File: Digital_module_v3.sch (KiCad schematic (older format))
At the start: 74 parts, among them J1 Pow_mng_iface, J2 Fan_mod_iface, J3 Iface_mod_iface, J4 B2B-EH-A, J5 ADC_iface, J6 USB_B_Micro, J7 Pow_mng_pow, J8 DS18B20_iface, Q1 BSS138, Q10 BSS138, Q11 BSS138, Q12 BSS138, Q2 BSS138, Q3 BSS138, Q4 BSS138, Q5 BSS138, Q6 BSS138, Q7 BSS138, Q8 BSS138, Q9 BSS138, U1 PCA9544APW, U2 PCF8563TS, U3 LM1117-3.3, U4 USBLC6-2SC6, Y1 SC-32S 32.768KHz

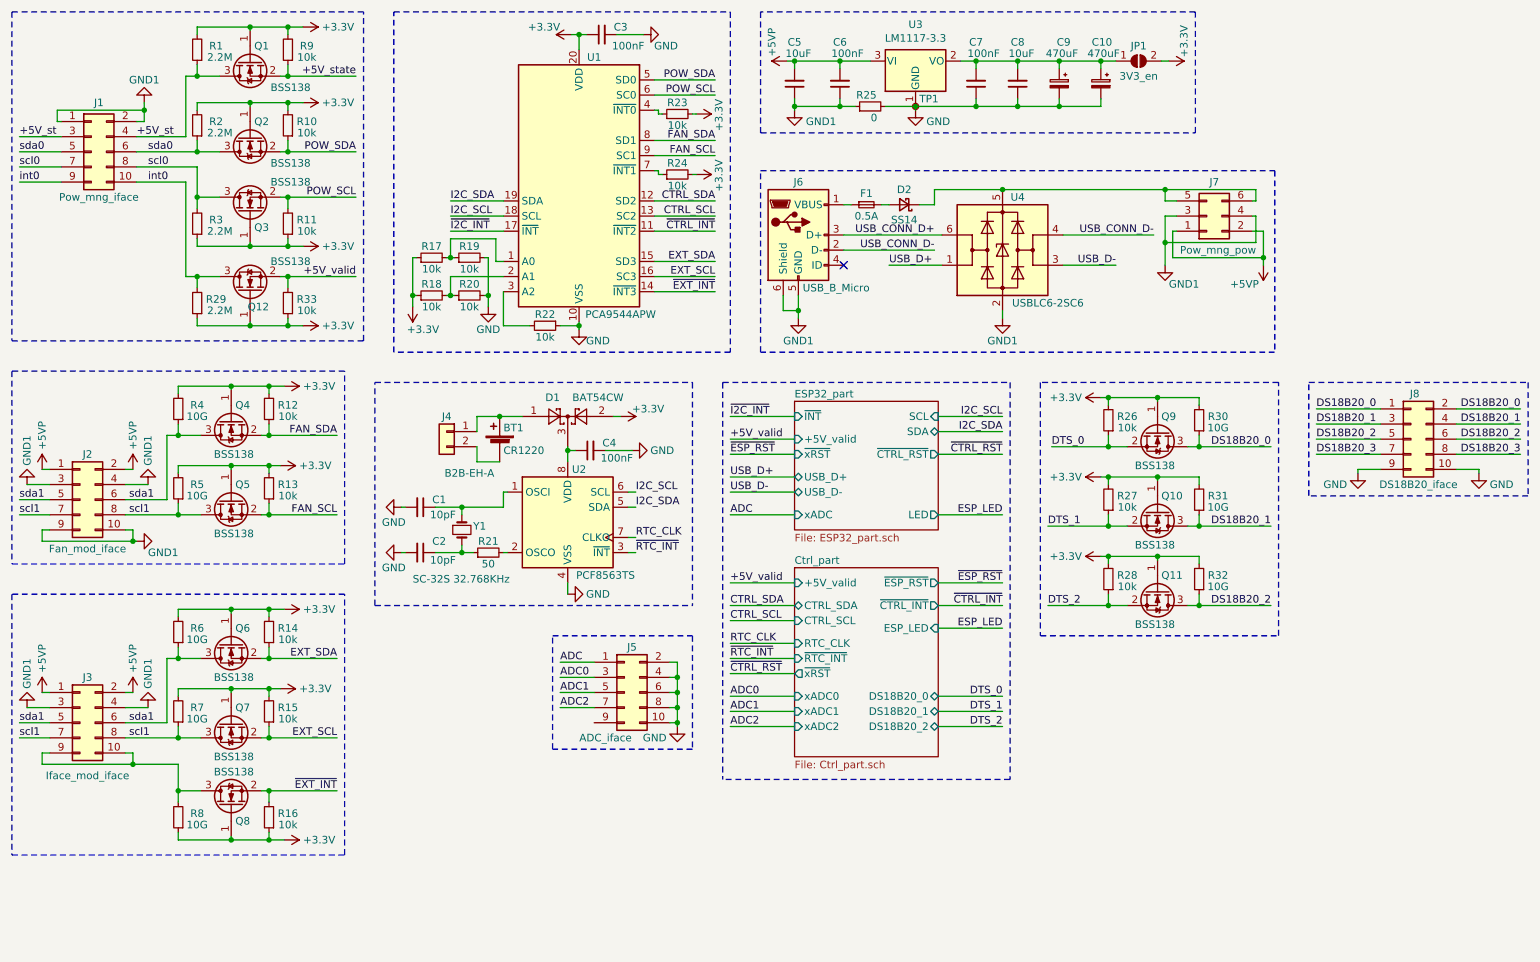
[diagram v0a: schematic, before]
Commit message: Завершена трассировка печатной платы. Исправлены ошибки в схема.
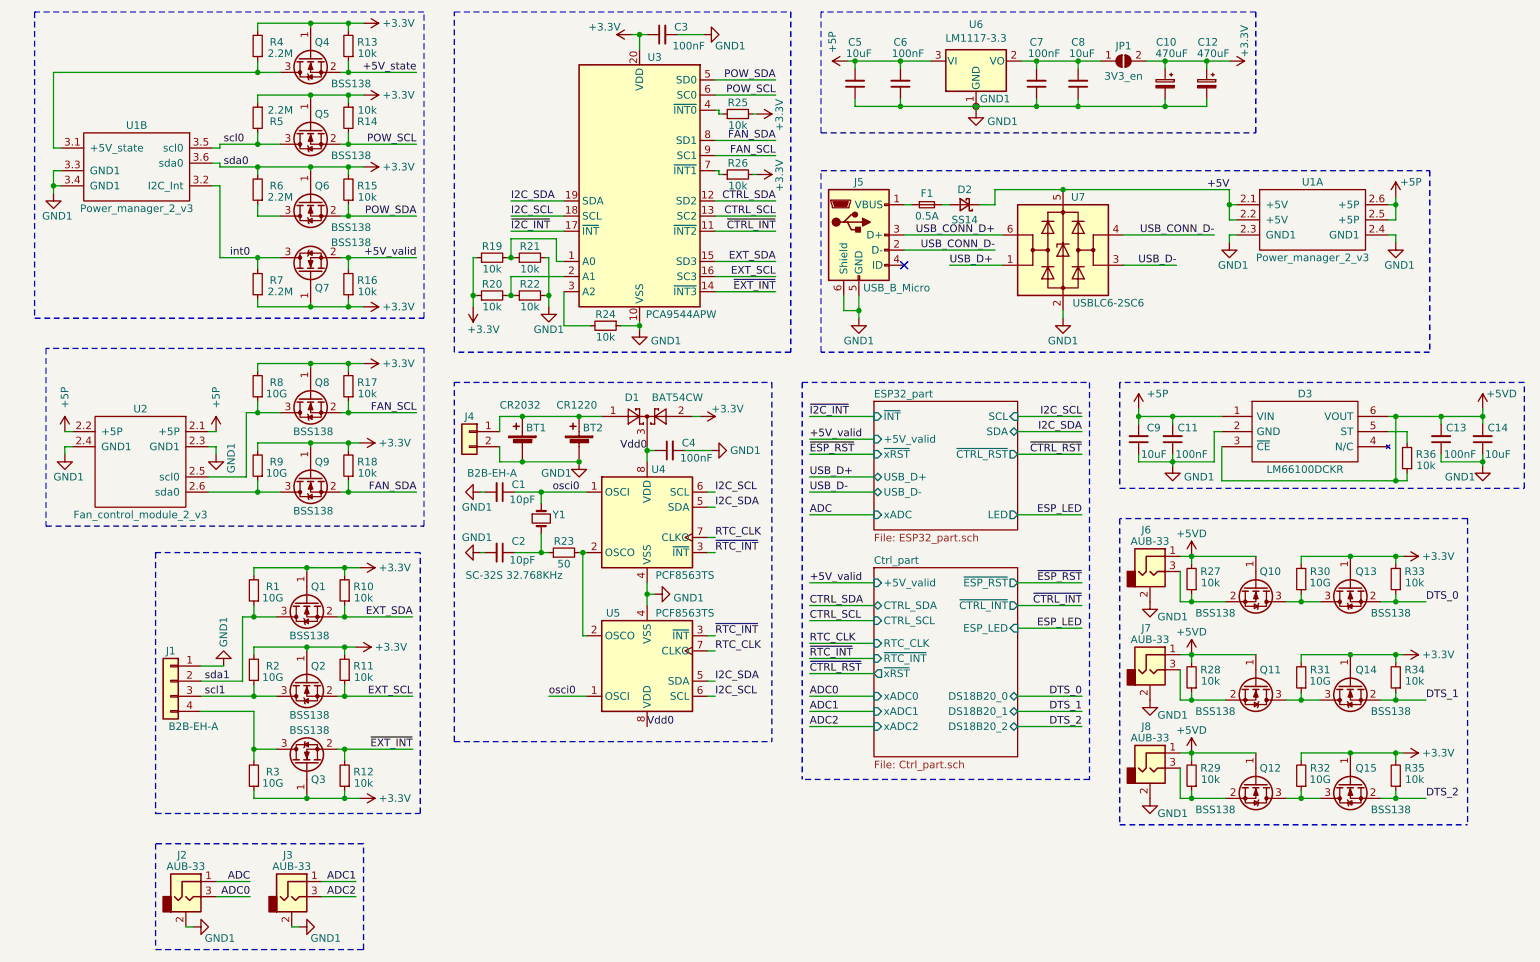
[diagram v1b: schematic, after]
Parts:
- removed J1: Pow_mng_iface, Connector_PinHeader_1.27mm:PinHeader_2x05_P1.27mm_Vertical_SMD, symbol Connector_Generic:Conn_02x05_Odd_Even
- removed J2: Fan_mod_iface, Connector_PinSocket_1.27mm:PinSocket_2x05_P1.27mm_Horizontal, symbol Connector_Generic:Conn_02x05_Odd_Even
- removed J3: Iface_mod_iface, Connector_PinSocket_1.27mm:PinSocket_2x05_P1.27mm_Horizontal, symbol Connector_Generic:Conn_02x05_Odd_Even
- removed J5: ADC_iface, Connector_PinSocket_1.27mm:PinSocket_2x05_P1.27mm_Horizontal, symbol Connector_Generic:Conn_02x05_Odd_Even
- removed J7: Pow_mng_pow, Connector_PinHeader_1.27mm:PinHeader_2x03_P1.27mm_Vertical_SMD, symbol Connector_Generic:Conn_02x03_Odd_Even
- removed J8: DS18B20_iface, Connector_PinSocket_1.27mm:PinSocket_2x05_P1.27mm_Horizontal, symbol Connector_Generic:Conn_02x05_Odd_Even
- removed Q9: BSS138, Package_TO_SOT_SMD:SOT-23, symbol Transistor_FET:BSS138
- removed R25: 0, Resistor_SMD:R_0603_1608Metric, symbol Device:R_Small
- removed R26: 10k, Resistor_SMD:R_0603_1608Metric, symbol Device:R_Small
- added BT1: CR2032, Modules:CR2032BS51, symbol Device:Battery_Cell
- added C11, C13: 100nF, Capacitor_SMD:C_0603_1608Metric, symbol Device:C_Small
- added C14, C9: 10uF, Capacitor_SMD:C_0603_1608Metric, symbol Device:C_Small
- added D3: LM66100DCKR, SOP65P210X110-6N, symbol Modules:LM66100DCKR
- added J1: B2B-EH-A, Connector_JST:JST_EH_S4B-EH_1x04_P2.50mm_Horizontal, symbol Connector_Generic:Conn_01x04
- added J2, J3, J6, J7, J8: AUB-33, Modules:AUB-33, symbol Modules:AUB-33
- added Q12, Q13, Q14, Q15: BSS138, Package_TO_SOT_SMD:SOT-23, symbol Transistor_FET:BSS138
- added R29, R33, R34, R35, R36: 10k, Resistor_SMD:R_0603_1608Metric, symbol Device:R_Small
- added U1: Power_manager_2_v3, Modules:Power_manager_2_v3, symbol Modules:Power_manager_2_v3
- added U2: Fan_control_module_2_v3, Modules:Fan_controller_2_v3, symbol Modules:Fan_control_module_2_v3
- added U5: PCF8563TS, Package_SO:SO-8_3.9x4.9mm_P1.27mm, symbol Timer_RTC:PCF8563TS
- GND1: renamed from TP1; value GND -> GND1
- renumbered BT1 to BT2, C9 to C10, C10 to C12, J6 to J5, Q6 to Q1, Q7 to Q2, Q8 to Q3, Q1 to Q4, Q3 to Q5, Q2 to Q6, Q12 to Q7, Q4 to Q8, Q5 to Q9, R6 to R1, R14 to R10, R15 to R11, R16 to R12, R9 to R13, R11 to R14, R10 to R15, R33 to R16, R12 to R17, R13 to R18, R17 to R19, R7 to R2, R18 to R20, R19 to R21, R20 to R22, R21 to R23, R22 to R24, R23 to R25, R24 to R26, R8 to R3, R1 to R4, R3 to R5, R2 to R6, R29 to R7, R4 to R8, R5 to R9, U1 to U3, U2 to U4, U3 to U6, U4 to U7
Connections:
- net GND is gone; now on net GND1: C1.2, C10.2, C12.2, C2.2, C3.2, C4.2, C7.1, C8.1, GND1.1, R21.2, R22.2, R24.1, U3.10 (VSS), U4.4 (VSS), U6.1 (GND)
- net +3V3: now also C10.1, C12.1, Q13.1 (G), Q14.1 (G), Q15.1 (G), R33.2, R34.2, R35.2, U1.3.6 (sda0); no longer Q10.1 (G), Q11.1 (G), R27.2, R28.2
- net ADC: now also J2.1
- net ADC0: now also J2.3
- net ADC1: now also J3.1
- net ADC2: now also J3.3
- net DTS_0: now also Q13.2 (S), R33.1
- net DTS_1: now also Q14.2 (S), R34.1; no longer Q10.2 (S), R27.1
- net DTS_2: now also Q15.2 (S), R35.1; no longer Q11.2 (S), R28.1
- net FAN_SCL: now also Q8.2 (S), R17.1; no longer Q9.2 (S), R18.1
- net FAN_SDA: now also Q9.2 (S), R18.1; no longer Q8.2 (S), R17.1
- net GND1: now also BT2.2 (-), J4.2 (Pin_2), BT1.2 (-), C11.1, C13.1, C14.1, C9.1, D3.2 (GND), J1.1 (Pin_1), J2.2, J3.2, J6.2, J7.2, J8.2, U1.2.3 (GND1), U1.2.4 (GND1), U1.3.3 (GND1), U1.3.4 (GND1), U2.2.3 (GND1), U2.2.4 (GND1), U5.4 (VSS)
- net I2C_SCL: now also U5.6 (SCL)
- net I2C_SDA: now also U5.5 (SDA)
- net RTC_CLK: now also U5.7 (CLKO)
- net int0: now also U1.3.2 (I2C_Int)
- net scl0: now also U1.3.5 (scl0)
- net scl1: now also J1.3 (Pin_3); no longer Q9.3 (D), R9.1
- net sda1: now also J1.2 (Pin_2); no longer Q8.3 (D), R8.1
- net ~RTC_INT: now also U5.3 (~INT~)
- net +5V: now reaches D2.1 (K), U7.5 (VBUS)
- net +5V: now also U1.2.1 (+5V), U1.2.2 (+5V)
- net at C7.2, C8.2, JP1.1 (A)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: no longer C10.1, C12.1
- net at Q3.3 (D), R3.2: now also J1.4 (Pin_4)
- net osci0: now reaches C1.1, U4.1 (OSCI), Y1.1
- net osci0: now also U5.1 (OSCI)
- net at R23.2, U4.2 (OSCO): now also U5.2 (OSCO)
- net Vdd0: now reaches C4.1, D1.3, U4.8 (VDD)
- net Vdd0: now also U5.8 (VDD)
- net at BT2.1 (+), D1.1, J4.1 (Pin_1): now also BT1.1 (+)
- net +5VP renamed +5P
- net +5P: now also C11.2, C9.2, D3.1 (VIN), U1.2.5 (+5P), U1.2.6 (+5P), U2.2.1 (+5P), U2.2.2 (+5P)
- net +5V_st: no longer names the net of Q4.3 (D), R4.1
- net +5V_st: now also U1.3.1 (+5V_state)
- net DS18B20_0: no longer names the net of R30.1
- net DS18B20_0: now also Q10.3 (D), Q13.3 (D)
- net DS18B20_1: no longer names the net of R31.1
- net DS18B20_1: now also Q11.3 (D), Q14.3 (D); no longer Q10.3 (D)
- net DS18B20_2: no longer names the net of R32.1
- net DS18B20_2: now also Q12.3 (D), Q15.3 (D); no longer Q11.3 (D)
- net sda0: no longer names the net of Q6.3 (D), R6.1
- new net: Q8.3 (D), R8.1, U2.2.5 (scl0)
- new net: Q9.3 (D), R9.1, U2.2.6 (sda0)
- new net: D3.5 (ST), R36.2
- new net: J6.3, Q10.2 (S), R27.1
- new net: J7.3, Q11.2 (S), R28.1
- new net: J8.3, Q12.2 (S), R29.1
- new net +5VD: C13.2, C14.2, D3.3 (~CE), D3.6 (VOUT), J6.1, J7.1, J8.1, Q10.1 (G), Q11.1 (G), Q12.1 (G), R27.2, R28.2, R29.2, R36.1
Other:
- moved on the sheet: BT2, C1, C10, C12, C2, C3, C4, C5, C6, C7, C8, D1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

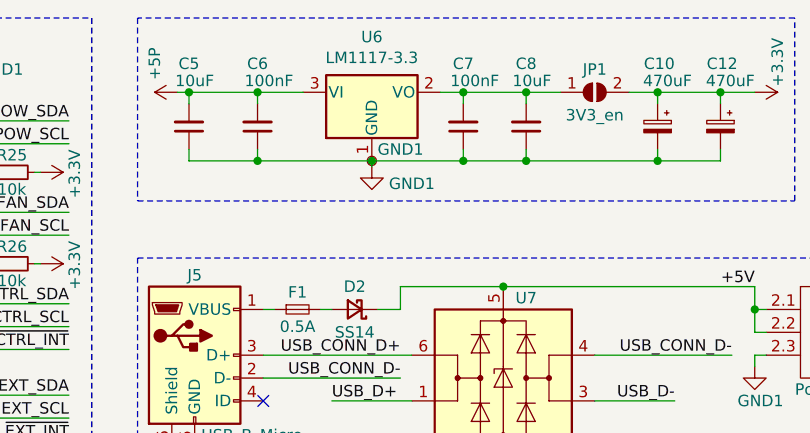
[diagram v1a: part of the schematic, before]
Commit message: Сформирован перечень элементов, 3D-модель, исправлены ошибки, реализована панелизация платы.
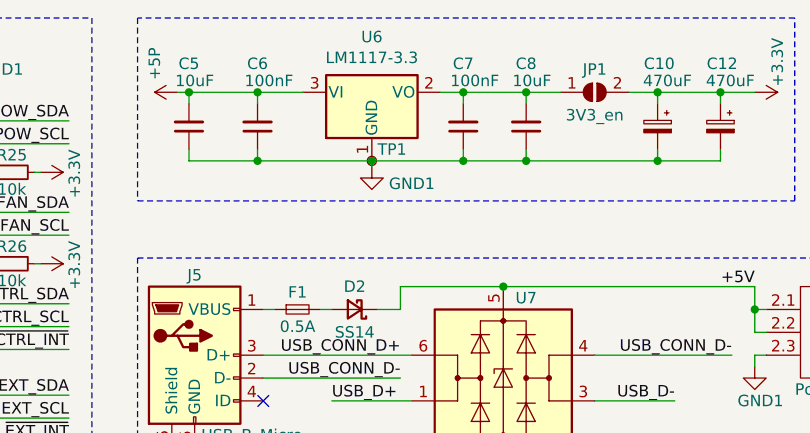
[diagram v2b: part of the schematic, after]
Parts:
- renumbered GND1 to TP1
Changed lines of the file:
@@
 P 7125 1375
 AR Path="/61767BB5/61554169/6178D3D0" Ref="TP?"  Part="1"
-AR Path="/6178D3D0" Ref="GND1"  Part="1"
-F 0 "GND1" H 7150 1425 50  0000 L CNN
+AR Path="/6178D3D0" Ref="TP1"  Part="1"
+F 0 "TP1" H 7150 1425 50  0000 L CNN
 F 1 "GND1" H 7050 1300 50  0001 L CNN
 F 2 "TestPoint:TestPoint_THTPad_D2.0mm_Drill1.0mm" H 7325 1375 50  0001 C CNN

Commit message: Последние изменения в BOM
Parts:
- J1: value B2B-EH-A -> B4B-EH-A
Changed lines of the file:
@@
 AR Path="/61554169/6173C66C/6495A185/61F064B4" Ref="J?"  Part="1"
 F 0 "J1" H 1800 5375 50  0000 C CNN
-F 1 "B2B-EH-A" H 1650 4875 50  0000 C CNN
+F 1 "B4B-EH-A" H 1650 4875 50  0000 C CNN
 F 2 "Connector_JST:JST_EH_S4B-EH_1x04_P2.50mm_Horizontal" H 1800 5175 50  0001 C CNN
 F 3 "~" H 1800 5175 50  0001 C CNN
